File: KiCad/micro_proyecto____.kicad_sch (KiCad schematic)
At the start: 12 parts, among them J2 Conn_01x03, J2 Conn_01x05, SW1 SW_Push, U4 PIC24HJ128GP502, Y1 Crystal

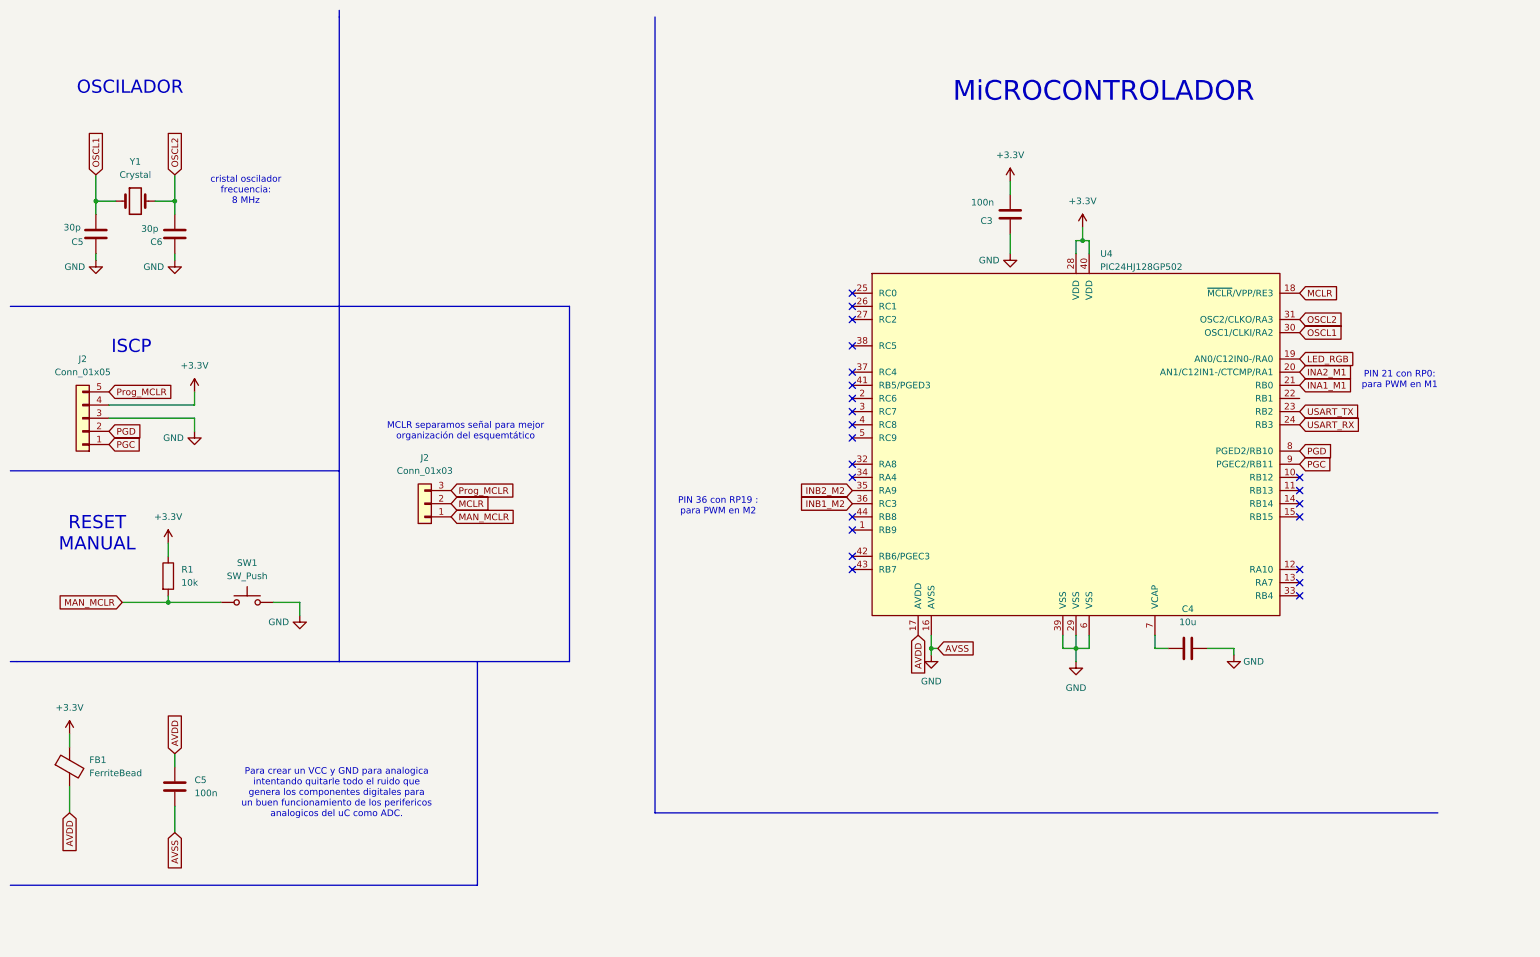
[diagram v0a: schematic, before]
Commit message: Actualización ESquematico arreglandolo y corrigiendo fallos
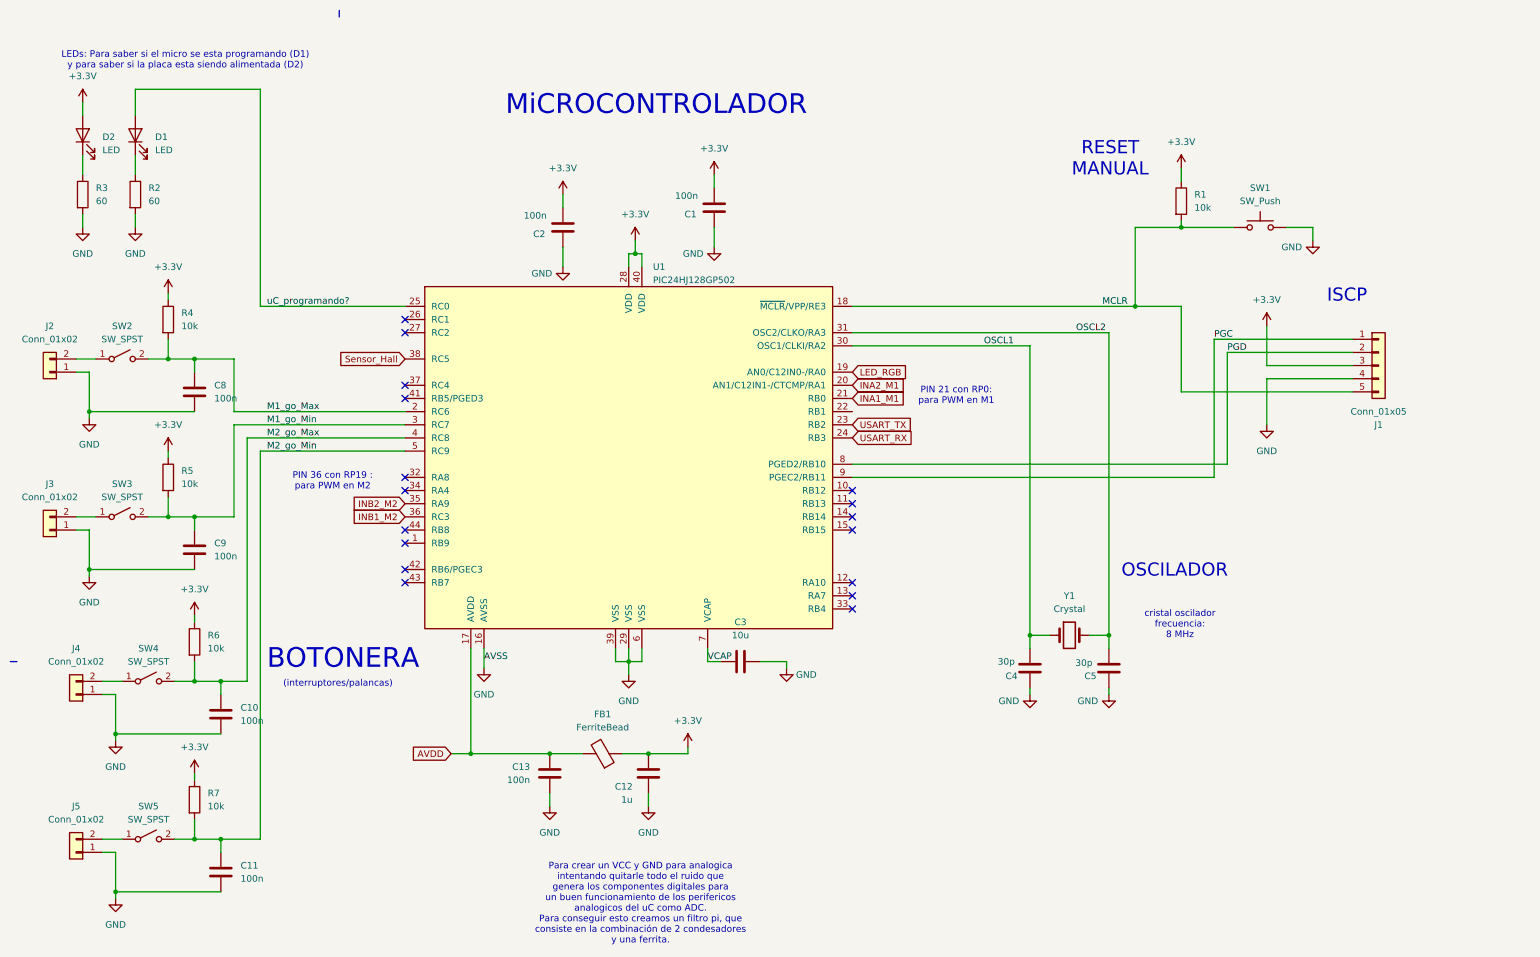
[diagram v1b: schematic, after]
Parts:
- removed C5: 100n, symbol Device:C
- removed J2: Conn_01x03, symbol Connector_Generic:Conn_01x03
- added C1, C10, C11, C13, C8, C9: 100n, symbol Device:C
- added C12: 1u, symbol Device:C
- added D1, D2: LED, symbol Device:LED
- added J2, J3, J4, J5: Conn_01x02, symbol Connector_Generic:Conn_01x02
- added R2, R3: 60, symbol Device:R
- added R4, R5, R6, R7: 10k, symbol Device:R
- added SW2, SW3, SW4, SW5: SW_SPST, symbol Switch:SW_SPST
- renumbered C3 to C2, C4 to C3, C5 to C4, C6 to C5, J2 to J1, U4 to U1
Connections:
- net MAN_MCLR is gone; now on net MCLR: R1.2, SW1.1
- net Prog_MCLR is gone; now on net MCLR: J1.5 (Pin_5)
- net +3.3V: now also J1.3 (Pin_3), C1.2, C12.1, D2.2 (A), R4.1, R5.1, R6.1, R7.1; no longer J1.4 (Pin_4)
- net AVDD: now also C13.1
- net GND: now also J1.4 (Pin_4), C1.1, C10.2, C11.2, C12.2, C13.2, C8.2, C9.2, J2.1 (Pin_1), J3.1 (Pin_1), J4.1 (Pin_1), J5.1 (Pin_1), R2.2, R3.2; no longer J1.3 (Pin_3)
- net VCAP: now reaches C3.2, U1.7 (VCAP)
- net M1_go_Max: now reaches U1.2 (RC6)
- net M1_go_Max: now also C8.1, R4.2, SW2.2 (B)
- net uC_programando?: now reaches U1.25 (RC0)
- net uC_programando?: now also D1.2 (A)
- net M1_go_Min: now reaches U1.3 (RC7)
- net M1_go_Min: now also C9.1, R5.2, SW3.2 (B)
- net Sensor_Hall: now reaches U1.38 (RC5)
- net M2_go_Max: now reaches U1.4 (RC8)
- net M2_go_Max: now also C10.1, R6.2, SW4.2 (B)
- net M2_go_Min: now reaches U1.5 (RC9)
- net M2_go_Min: now also C11.1, R7.2, SW5.2 (B)
- new net: J4.2 (Pin_2), SW4.1 (A)
- new net: D1.1 (K), R2.1
- new net: J5.2 (Pin_2), SW5.1 (A)
- new net: D2.1 (K), R3.1
- new net: J2.2 (Pin_2), SW2.1 (A)
- new net: J3.2 (Pin_2), SW3.1 (A)
- no-connect marks 23 -> 17
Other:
- note added: "(interruptores/palancas)"
- note added: "BOTONERA"
- note added: "LEDs: Para saber si el micro se esta programando (D1) y para saber si la placa esta siendo alimentada (D2)"
- note added: "Para crear un VCC y GND para analogica intentando quitarle todo el ruido que genera los componentes digitales para un buen funcionamiento de los perifericos analogicos del uC como ADC. Para conseguir esto creamos un filtro pi, que consiste en la combinación de 2 condesadores y una ferrita."
- note removed: "MCLR separamos señal para mejor organización del esquemtático"
- note removed: "Para crear un VCC y GND para analogica intentando quitarle todo el ruido que genera los componentes digitales para un buen funcionamiento de los perifericos analogicos del uC como ADC."
- moved on the sheet: C2, C3, C4, C5, J1, R1, SW1, U1, Y1

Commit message: Nuevos cambios esquemativo v3
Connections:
- net I2C_SDA: now reaches U1.1 (RB9)
- net I2C_SCL: now reaches U1.44 (RB8)
- no-connect marks 17 -> 15
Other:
- moved on the sheet: C1, C10, C11, C12, C13, C2, C3, C4, C5, C8, C9, D1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

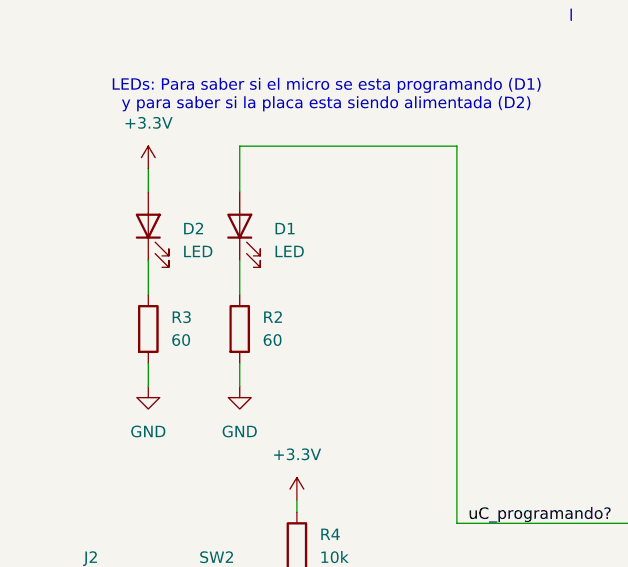
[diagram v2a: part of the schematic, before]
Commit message: Actualización de Esquematico, he puesto footprints y readme cambiado
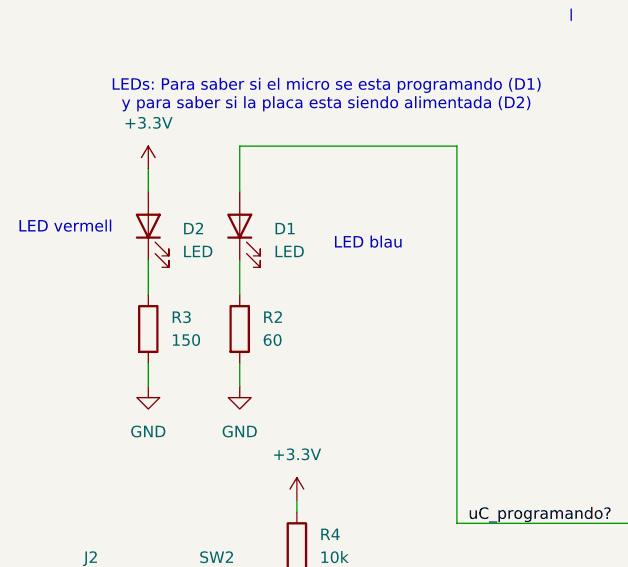
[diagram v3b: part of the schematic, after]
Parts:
- C1, C10, C11, C12, C13, C2, C3, C4, C5, C8, C9: footprint (none) -> Capacitor_SMD:C_0805_2012Metric
- D1, D2: footprint (none) -> LED_SMD:LED_0805_2012Metric
- FB1, R1, R2, R4, R5, R6, R7: footprint (none) -> Resistor_SMD:R_0805_2012Metric
- J1: footprint (none) -> Connector_PinHeader_2.54mm:PinHeader_1x05_P2.54mm_Vertical
- J2, J3, J4, J5: footprint (none) -> Connector_PinHeader_2.54mm:PinHeader_1x02_P2.54mm_Horizontal
- R3: value 60 -> 150; footprint (none) -> Resistor_SMD:R_0805_2012Metric
- SW1: footprint (none) -> Button_Switch_THT:SW_PUSH_6mm
- SW2, SW3, SW4, SW5: footprint (none) -> Button_Switch_THT:SW_SPST_Omron_B3F-50xx
- Y1: footprint (none) -> Crystal:Crystal_SMD_7050-2Pin_7.0x5.0mm_HandSoldering
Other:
- note added: "LED blau"
- note added: "LED vermell"
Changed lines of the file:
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@@
 		)
 	)
+	(text "LED vermell"
+		(exclude_from_sim no)
+		(at 13.462 35.814 0)
+		(effects
+			(font
+				(size 1.27 1.27)
+			)
+			(justify left)
+		)
+	)
 	(text "RESET \nMANUAL\n"
 		(exclude_from_sim no)
@@
 		)
 	)
+	(text "LED blau\n"
+		(exclude_from_sim no)
+		(at 48.514 37.592 0)
+		(effects
+			(font
+				(size 1.27 1.27)
+			)
+			(justify left)
+		)
+	)
 	(text "BOTONERA\n"
 		(exclude_from_sim no)
@@
 			)
 		)
-		(property "Footprint" ""
+		(property "Footprint" "Resistor_SMD:R_0805_2012Metric"
 			(at 42.672 101.6 90)
 			(effects
@@
 			)
 		)
-		(property "Footprint" ""
+		(property "Footprint" "Resistor_SMD:R_0805_2012Metric"
 			(at 128.27 156.718 90)
 			(effects
@@
 			)
 		)
-		(property "Footprint" ""
+		(property "Footprint" "Capacitor_SMD:C_0805_2012Metric"
 			(at 148.8948 45.72 0)
 			(effects
@@
 			)
 		)
-		(property "Footprint" ""
+		(property "Footprint" "Capacitor_SMD:C_0805_2012Metric"
 			(at 136.1948 162.56 0)
 			(effects
@@
 			)
 		)
-		(property "Footprint" ""
+		(property "Footprint" "Connector_PinHeader_2.54mm:PinHeader_1x02_P2.54mm_Horizontal"
 			(at 26.67 143.51 0)
 			(effects
@@
 			)
 		)
-		(property "Footprint" ""
+		(property "Footprint" "LED_SMD:LED_0805_2012Metric"
 			(at 38.1 35.56 0)
 			(effects
@@
 			)
 		)
-		(property "Footprint" ""
+		(property "Footprint" "Capacitor_SMD:C_0805_2012Metric"
 			(at 50.4952 119.38 0)
 			(effects
@@
 			)
 		)
-		(property "Footprint" ""
+		(property "Footprint" "Capacitor_SMD:C_0805_2012Metric"
 			(at 117.1448 162.56 0)
 			(effects
@@
 			)
 		)
-		(property "Footprint" ""
+		(property "Footprint" "Capacitor_SMD:C_0805_2012Metric"
 			(at 225.0948 134.62 0)
 			(effects
@@
 			)
 		)
-		(property "Footprint" ""
+		(property "Footprint" "Connector_PinHeader_2.54mm:PinHeader_1x05_P2.54mm_Vertical"
 			(at 278.13 80.01 0)
 			(effects
@@
 			)
 		)
-		(property "Footprint" ""
+		(property "Footprint" "Capacitor_SMD:C_0805_2012Metric"
 			(at 209.8548 134.62 0)
 			(effects
@@
 			)
 		)
-		(property "Footprint" ""
+		(property "Footprint" "Button_Switch_THT:SW_SPST_Omron_B3F-50xx"
 			(at 40.64 171.45 0)
 			(effects
@@
 			)
 		)
-		(property "Value" "60"
+		(property "Value" "150"
 			(at 30.48 48.2599 0)
 			(effects
@@
 			)
 		)
-		(property "Footprint" ""
+		(property "Footprint" "Resistor_SMD:R_0805_2012Metric"
 			(at 26.162 46.99 90)
 			(effects
@@
 			)
 		)
-		(property "Footprint" ""
+		(property "Footprint" "Resistor_SMD:R_0805_2012Metric"
 			(at 238.252 48.26 90)
 			(effects
@@
 			)
 		)
-		(property "Footprint" ""
+		(property "Footprint" "Resistor_SMD:R_0805_2012Metric"
 			(at 47.752 133.35 90)
 			(effects
@@
 			)
 		)
-		(property "Footprint" ""
+		(property "Footprint" "Button_Switch_THT:SW_SPST_Omron_B3F-50xx"
 			(at 35.56 78.74 0)
 			(effects
@@
 			)
 		)
-		(property "Footprint" ""
+		(property "Footprint" "Resistor_SMD:R_0805_2012Metric"
 			(at 47.752 163.83 90)
 			(effects
@@
 			)
 		)
-		(property "Footprint" ""
+		(property "Footprint" "Resistor_SMD:R_0805_2012Metric"
 			(at 42.672 71.12 90)
 			(effects
@@
 			)
 		)
-		(property "Footprint" ""
+		(property "Footprint" "Connector_PinHeader_2.54mm:PinHeader_1x02_P2.54mm_Horizontal"
 			(at 21.59 81.28 0)
 			(effects
@@
 			)
 		)
-		(property "Footprint" ""
+		(property "Footprint" "Connector_PinHeader_2.54mm:PinHeader_1x02_P2.54mm_Horizontal"
 			(at 21.59 111.76 0)
 			(effects
@@
 			)
 		)
-		(property "Footprint" ""
+		(property "Footprint" "Button_Switch_THT:SW_SPST_Omron_B3F-50xx"
 			(at 40.64 140.97 0)
 			(effects
@@
 			)
 		)
-		(property "Footprint" ""
+		(property "Footprint" "Crystal:Crystal_SMD_7050-2Pin_7.0x5.0mm_HandSoldering"
 			(at 218.44 132.08 0)
 			(effects
@@
 			)
 		)
-		(property "Footprint" ""
+		(property "Footprint" "LED_SMD:LED_0805_2012Metric"
 			(at 27.94 35.56 0)
 			(effects
@@
 			)
 		)
-		(property "Footprint" ""
+		(property "Footprint" "Capacitor_SMD:C_0805_2012Metric"
 			(at 55.5752 181.61 0)
 			(effects
@@
 			)
 		)
-		(property "Footprint" ""
+		(property "Footprint" "Capacitor_SMD:C_0805_2012Metric"
 			(at 119.6848 49.53 0)
 			(effects
@@
 			)
 		)
-		(property "Footprint" ""
+		(property "Footprint" "Capacitor_SMD:C_0805_2012Metric"
 			(at 50.4952 88.9 0)
 			(effects
@@
 			)
 		)
-		(property "Footprint" ""
+		(property "Footprint" "Capacitor_SMD:C_0805_2012Metric"
 			(at 151.13 138.1252 0)
 			(effects
@@
 			)
 		)
-		(property "Footprint" ""
+		(property "Footprint" "Resistor_SMD:R_0805_2012Metric"
 			(at 36.322 46.99 90)
 			(effects
@@
 			)
 		)
-		(property "Footprint" ""
+		(property "Footprint" "Button_Switch_THT:SW_PUSH_6mm"
 			(at 255.27 48.26 0)
 			(effects
@@
 			)
 		)
-		(property "Footprint" ""
+		(property "Footprint" "Button_Switch_THT:SW_SPST_Omron_B3F-50xx"
 			(at 35.56 109.22 0)
 			(effects
@@
 			)
 		)
-		(property "Footprint" ""
+		(property "Footprint" "Capacitor_SMD:C_0805_2012Metric"
 			(at 55.5752 151.13 0)
 			(effects
@@
 			)
 		)
-		(property "Footprint" ""
+		(property "Footprint" "Connector_PinHeader_2.54mm:PinHeader_1x02_P2.54mm_Horizontal"
 			(at 26.67 173.99 0)
 			(effects
